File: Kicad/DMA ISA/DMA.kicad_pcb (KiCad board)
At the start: 2 copper layers, 132 x 73.9 mm, 18 parts, among them J1 Conn_02x08_Counter_Clockwise, J9 Bus_ISA_8bit, U1 74LS04, U2 74LS573, U3 74LS670, U4 8237, U5 74LS139

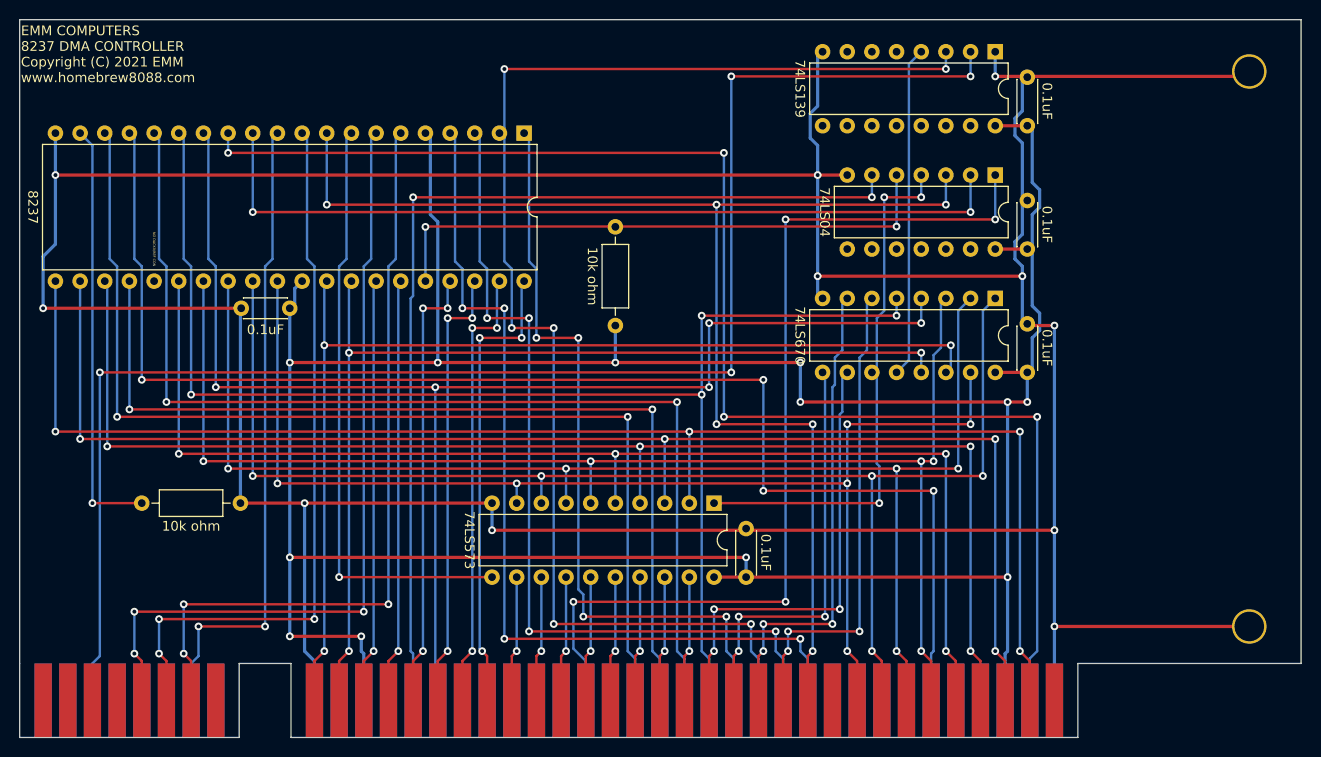
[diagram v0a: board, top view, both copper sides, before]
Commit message: Update to DMA card
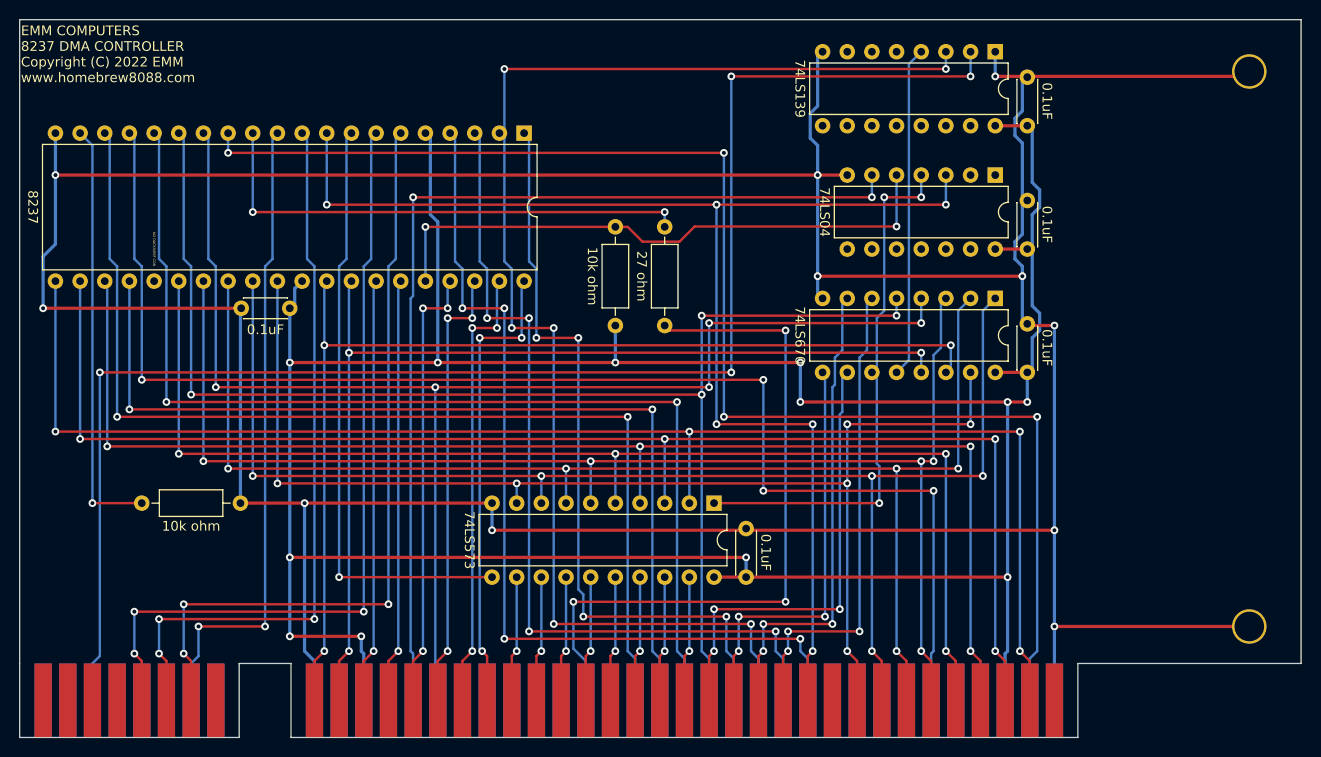
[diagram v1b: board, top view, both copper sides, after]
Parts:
- added R3: 27 ohm, Resistor_THT:R_Axial_DIN0207_L6.3mm_D2.5mm_P10.16mm_Horizontal, F.Cu at (121.4, 81.0)
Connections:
- U1 pad 1: /CLK88 -> Net-(U1-Pad1)
- U1 pad 2: /CLK88_1 -> Net-(U1-Pad2)
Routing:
- net /CLK88_1: track 85.9 -> 52.1 mm
- net /CLK88: track 98.1 -> 73.1 mm, vias 4 -> 3
- net /EOP: track 59.4 -> 60.7 mm
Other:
- board text added: "EMM COMPUTERS 8237 DMA CONTROLLER Copyright (C) 2022 EMM www.homebrew8088.com"
- board text removed: "EMM COMPUTERS 8237 DMA CONTROLLER Copyright (C) 2021 EMM www.homebrew8088.com"

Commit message: DMA update
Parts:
- U4: renamed from U3; value 74LS670 -> 74LS04
- U5: renamed from U2; value 74LS573 -> 74LS139
- renumbered U4 to U1, U5 to U2, U1 to U3

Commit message: Gerber update
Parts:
- U4: value 74LS04 -> 74LS670
- U5: value 74LS139 -> 74LS573
- renumbered C8 to C5

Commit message: Updated DMA card
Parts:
- moved C1 84.4 mm to (77.8, 89.4), turned to 0 degrees
- moved C2 84.4 mm to (158.7, 65.6), turned to 270 degrees
- renumbered R2 to R1, R1 to R2
